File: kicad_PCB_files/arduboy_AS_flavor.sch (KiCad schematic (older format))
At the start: 70 parts, among them J1 USB_B_Micro, Q1 Si2301CDS, Q2 2N7002, SW1 RST Button, SW2 UP Button, SW3 DOWN Button, SW4 LEFT Button, SW5 RIGHT Button, SW6 RIGHT Button, SW7 RIGHT Button, SW8 ON Button, U1A1 ATmega32U4-AU, U1B1 ATmega32U4-MU, U2 TP4054, U3 W25Q128JVSIQ, Y1 16MHz

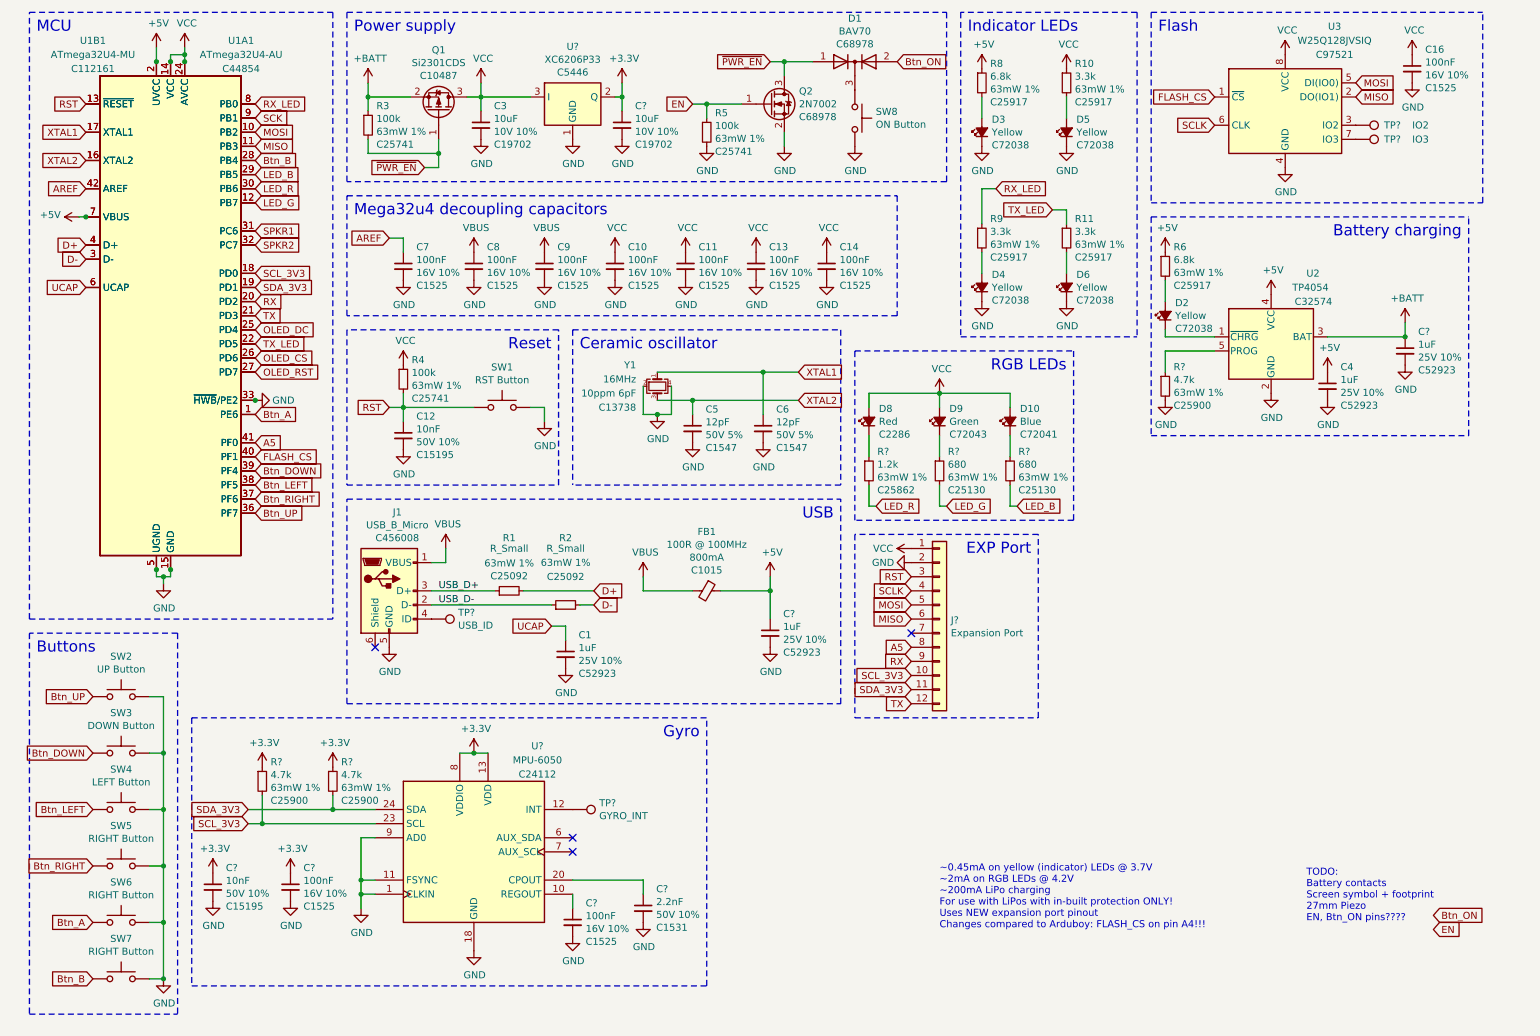
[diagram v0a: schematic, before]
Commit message: Multiple schematic changes Added SSH1106 connector (30 pin 0.7mm pitch)
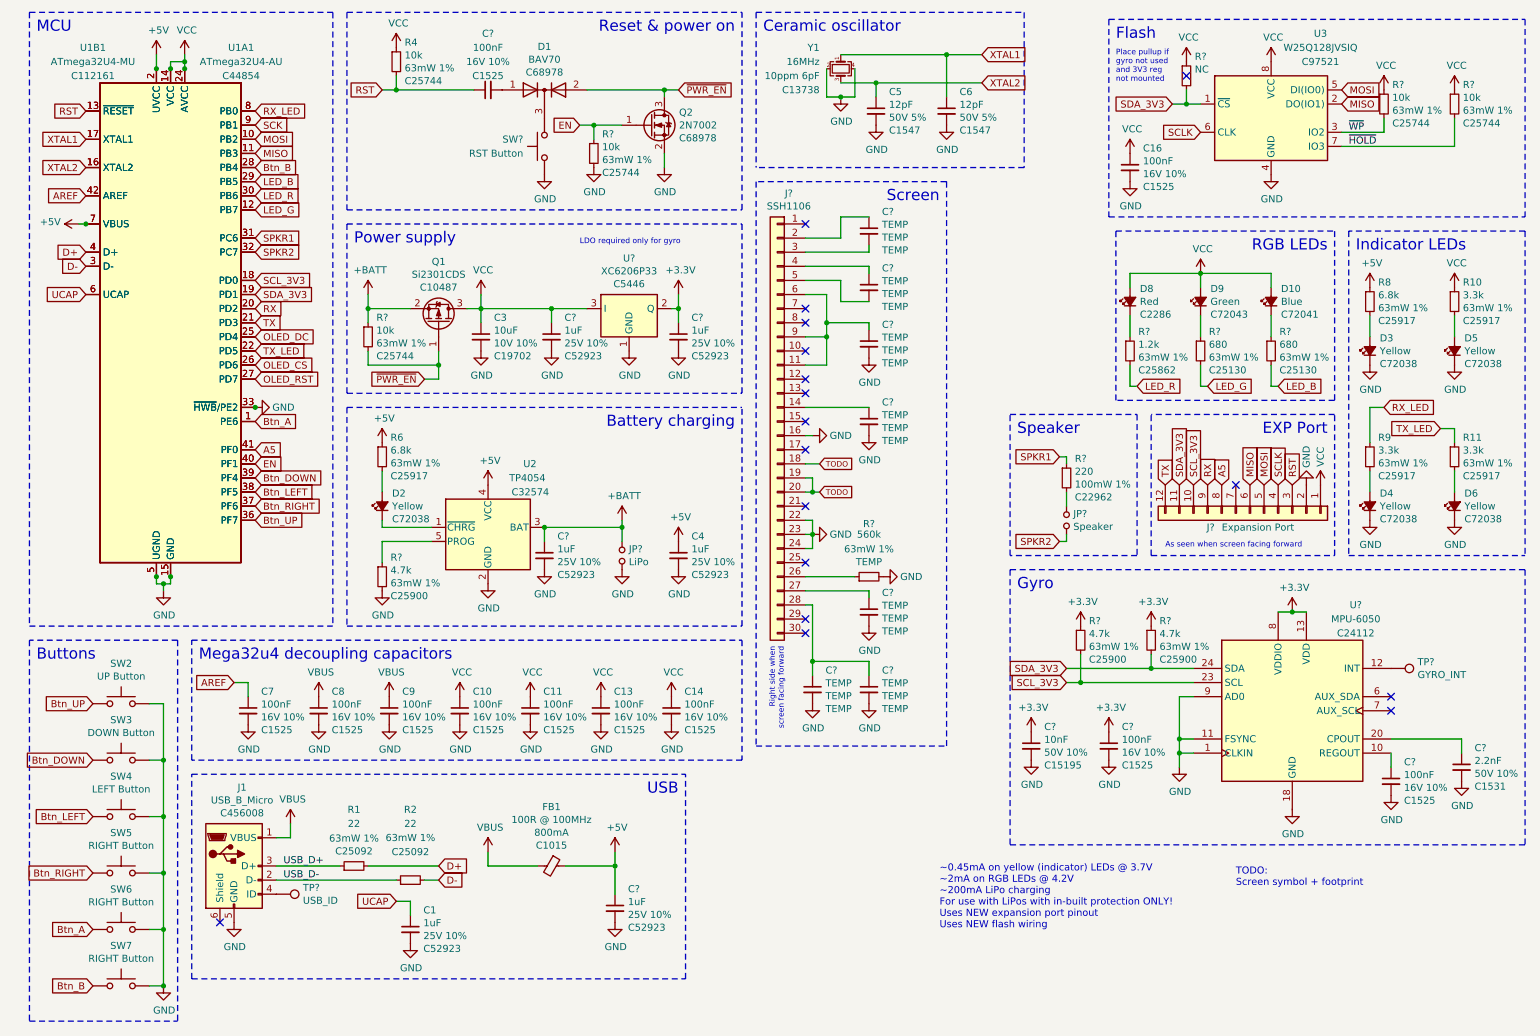
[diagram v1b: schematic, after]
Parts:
- removed C12: 10nF, Capacitor_SMD:C_0402_1005Metric_Pad0.74x0.62mm_HandSolder, symbol Device:C_Small
- removed C?: 10uF, Capacitor_SMD:C_0603_1608Metric_Pad1.08x0.95mm_HandSolder, symbol Device:C_Small
- removed R3, R5: 100k, Resistor_SMD:R_0402_1005Metric_Pad0.72x0.64mm_HandSolder, symbol Device:R_Small
- removed SW1: RST Button, arduboy:button_TS-1187A-B-A-B, symbol Switch:SW_Push
- removed SW8: ON Button, arduboy:button_TS-1187A-B-A-B, symbol Switch:SW_Push
- removed TP?: IO2, symbol Connector:TestPoint
- removed TP?: IO3, symbol Connector:TestPoint
- added C?: 100nF, Capacitor_SMD:C_0402_1005Metric_Pad0.74x0.62mm_HandSolder, symbol Device:C_Small
- added C? (x2): 1uF, Capacitor_SMD:C_0402_1005Metric_Pad0.74x0.62mm_HandSolder, symbol Device:C_Small
- added C? (x7): TEMP, Capacitor_SMD:C_0402_1005Metric_Pad0.74x0.62mm_HandSolder, symbol Device:C_Small
- added J?: SSH1106, arduboy:SSH1106_30pin_P0.7mm, symbol Connector_Generic:Conn_01x30
- added JP?: Speaker, symbol Device:Jumper_NO_Small
- added JP?: LiPo, symbol Device:Jumper_NO_Small
- added R?: NC, Resistor_SMD:R_0402_1005Metric_Pad0.72x0.64mm_HandSolder, symbol Device:R_Small
- added R? (x4): 10k, Resistor_SMD:R_0402_1005Metric_Pad0.72x0.64mm_HandSolder, symbol Device:R_Small
- added R?: 220, Resistor_SMD:R_0603_1608Metric_Pad0.98x0.95mm_HandSolder, symbol Device:R_Small
- added R?: 560k, Resistor_SMD:R_0402_1005Metric_Pad0.72x0.64mm_HandSolder, symbol Device:R_Small
- added SW?: RST Button, arduboy:button_TS-1187A-B-A-B, symbol Switch:SW_Push
- R1, R2: value R_Small -> 22
- R4: value 100k -> 10k; LCSC C25741 -> C25744
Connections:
- net Btn_ON is gone; now on net ~PWR_EN: D1.2 (A)
- net +3V3: now also C?.1
- net +BATT: now also JP?.2, R?.1
- net EN: now also U1A1.40 (PF1), U1B1.40 (PF1), R?.1
- net GND: now also C?.2, C?.2, C?.2, C?.2, C?.2, C?.2, C?.2, J?.16 (Pin_16), J?.22 (Pin_22), J?.23 (Pin_23), J?.24 (Pin_24), JP?.1, R?.2, R?.2, SW?.1
- net RST: now also C?.1
- net SDA_3V3: now also U3.1 (~CS), R?.2
- net SPKR1: now also R?.1
- net SPKR2: now also JP?.1
- net VCC: now also C?.1, R?.1, R?.1, R?.1
- net ~PWR_EN: now also R?.2; no longer D1.1 (A)
- net ~WP: now reaches U3.3 (IO2)
- net ~WP: now also R?.2
- net ~HOLD: now reaches U3.7 (IO3)
- net ~HOLD: now also R?.2
- net at D1.3 (K): now also SW?.2
- removed net FLASH_CS: U1A1.40 (PF1), U1B1.40 (PF1), U3.1 (~CS)
- new net: C?.2, D1.1 (A)
- new net: JP?.2, R?.2
- new net: C?.1, J?.11 (Pin_11), J?.6 (Pin_6), J?.9 (Pin_9)
- new net: C?.1, J?.14 (Pin_14)
- new net: C?.1, J?.2 (Pin_2)
- new net: J?.26 (Pin_26), R?.1
- new net: C?.1, J?.27 (Pin_27)
- new net: C?.1, C?.1, J?.28 (Pin_28)
- new net: C?.2, J?.3 (Pin_3)
- new net: C?.1, J?.4 (Pin_4)
- new net: C?.2, J?.5 (Pin_5)
- new net TODO: J?.18 (Pin_18), J?.19 (Pin_19), J?.20 (Pin_20)
- no-connect marks 4 -> 17
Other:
- note added: "As seen when screen facing forward"
- note added: "LDO required only for gyro"
- note added: "Place pullup if\ngyro not used\nand 3V3 reg\nnot mounted"
- note added: "Reset & power on"
- note added: "Right side when\nscreen facing forward"
- note added: "Screen"
- note added: "Speaker"
- note added: "TODO:\nScreen symbol + footprint"
- note added: "~~0.45mA on yellow (indicator) LEDs @ 3.7V\n~~2mA on RGB LEDs @ 4.2V\n~~200mA LiPo charging\nFor use with LiPos with in-built protection ONLY!\nUses NEW expansion port pinout\nUses NEW flash wiring"
- note removed: "Reset"
- note removed: "TODO:\nBattery contacts\nScreen symbol + footprint\n27mm Piezo\nEN, Btn_ON pins????"
- note removed: "~~0.45mA on yellow (indicator) LEDs @ 3.7V\n~~2mA on RGB LEDs @ 4.2V\n~~200mA LiPo charging\nFor use with LiPos with in-built protection ONLY!\nUses NEW expansion port pinout\nChanges compared to Arduboy: FLASH_CS on pin A4!!!"
- moved on the sheet: C1, C10, C11, C13, C14, C16, C3, C4, C5, C6, C7, C8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

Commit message: v0.1 schematic Added screen connectors Added testpoints Exported v0.1 schematic as .pdf
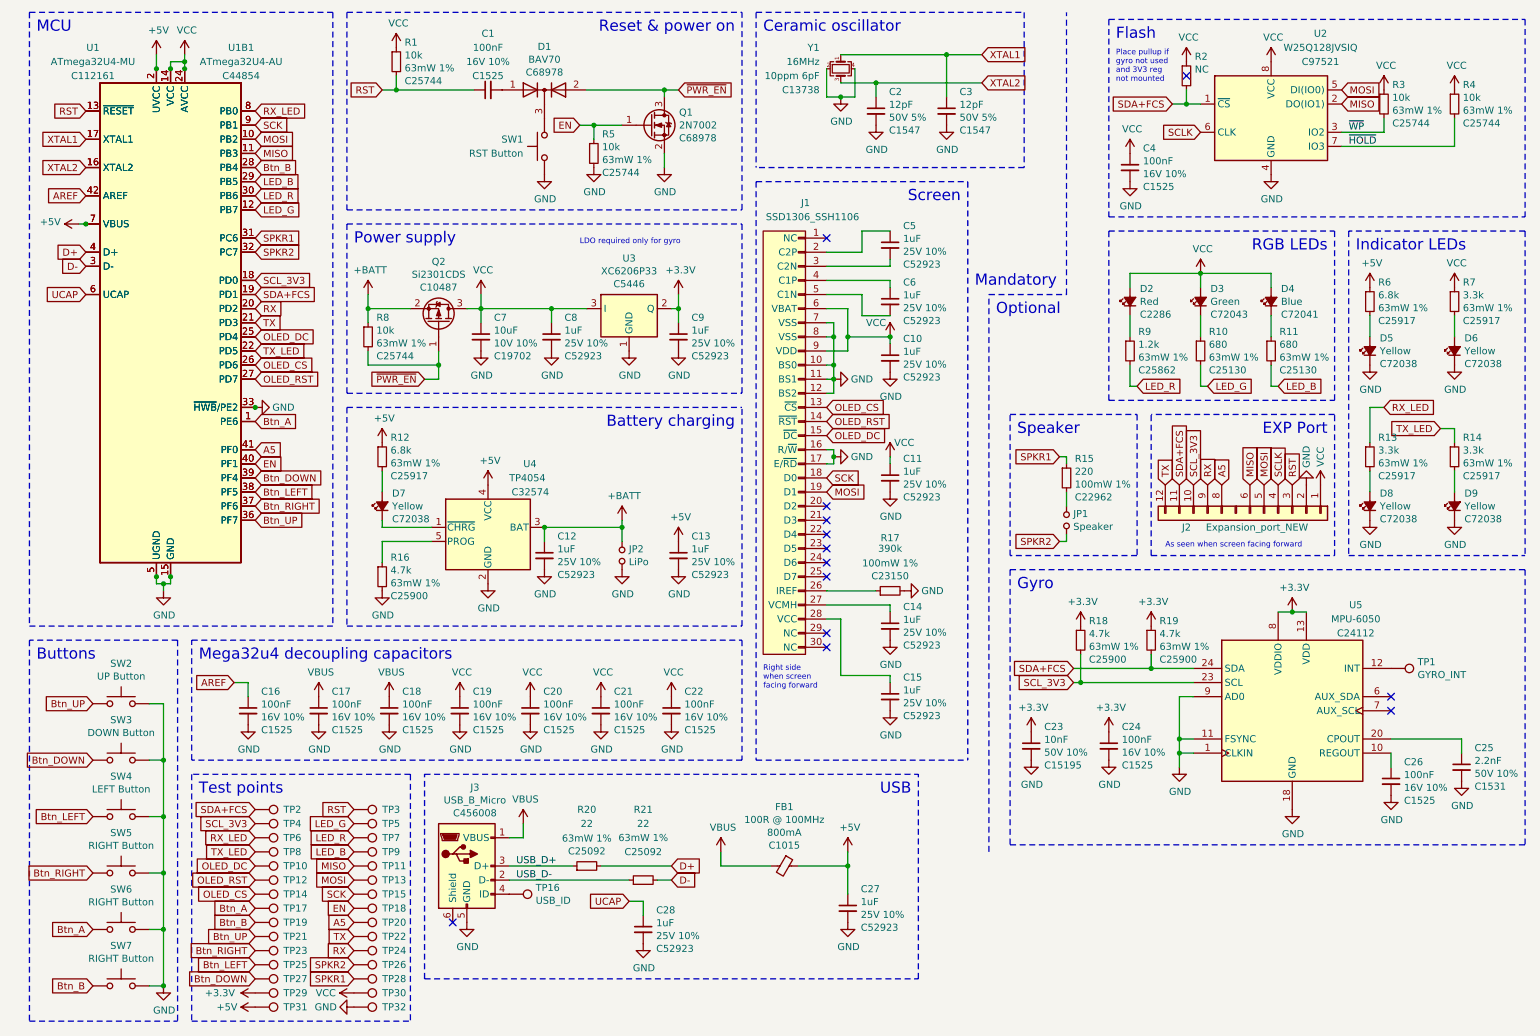
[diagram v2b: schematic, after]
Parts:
- removed C? (x7): TEMP, Capacitor_SMD:C_0402_1005Metric_Pad0.74x0.62mm_HandSolder, symbol Device:C_Small
- removed J?: SSH1106, arduboy:SSH1106_30pin_P0.7mm, symbol Connector_Generic:Conn_01x30
- removed J?: Expansion Port, symbol Connector_Generic:Conn_01x12
- added C10, C11, C14, C15, C5, C6: 1uF, Capacitor_SMD:C_0402_1005Metric_Pad0.74x0.62mm_HandSolder, symbol Device:C_Small
- added J1: SSD1306_SSH1106, arduboy:SSH1106_30pin_P0.7mm, symbol arduboy:SSD1306_SSH1106_30pin_soldered
- added J2: Expansion_port_NEW, arduboy:PinHeader_1x12_P2.54mm_SLOTTED_ROTATED, symbol arduboy:Expansion_port_NEW
- added TP10: D4/D4/~OLED_DC, symbol Connector:TestPoint
- added TP11: D14/PB3/MISO, symbol Connector:TestPoint
- added TP12: D6/D7/~OLED_RST, symbol Connector:TestPoint
- added TP13: D16/PB2/MOSI, symbol Connector:TestPoint
- added TP14: D12/D6/~OLED_CS, symbol Connector:TestPoint
- added TP15: D15/PB1/SCK, symbol Connector:TestPoint
- added TP17: D7/E6/A, symbol Connector:TestPoint
- added TP18: A4/F1/EN, symbol Connector:TestPoint
- added TP19: D8/PB4/B, symbol Connector:TestPoint
- added TP2: D2/PD1/SDA+FLASH_CS, symbol Connector:TestPoint
- added TP20: A5/F0, symbol Connector:TestPoint
- added TP21: A0/PF7/UP, symbol Connector:TestPoint
- added TP22: D1/PD3/TX, symbol Connector:TestPoint
- added TP23: A1/F6/RIGHT, symbol Connector:TestPoint
- added TP24: D0/PD2/RX, symbol Connector:TestPoint
- added TP25: A2/F5/LEFT, symbol Connector:TestPoint
- added TP26: D13/PC7/SPKR2, symbol Connector:TestPoint
- added TP27: A3/F4/DOWN, symbol Connector:TestPoint
- added TP28: D5/PC6/SPKR1, symbol Connector:TestPoint
- added TP29: 3V3, symbol Connector:TestPoint
- added TP3: ~RST, symbol Connector:TestPoint
- added TP30: VCC, symbol Connector:TestPoint
- added TP31: 5V_USB, symbol Connector:TestPoint
- added TP32: GND, symbol Connector:TestPoint
- added TP4: D3/PD0/SCL, symbol Connector:TestPoint
- added TP5: D11/PB7/~LED_G, symbol Connector:TestPoint
- added TP6: D17/PB0/~RX_LED, symbol Connector:TestPoint
- added TP7: D10/PB6/~LED_R, symbol Connector:TestPoint
- added TP8: D30/D5/~TX_LED, symbol Connector:TestPoint
- added TP9: D9/PB5/~LED_B, symbol Connector:TestPoint
- R17: renamed from R?; value 560k -> 390k; footprint Resistor_SMD:R_0402_1005Metric_Pad0.72x0.64mm_HandSolder -> Resistor_SMD:R_0603_1608Metric_Pad0.98x0.95mm_HandSolder; LCSC TEMP -> C23150; Rating 63mW 1% -> 100mW 1%
- gave numbers to parts that had none: 28
- renumbered C4 to C13, C7 to C16, C8 to C17, C9 to C18, C10 to C19, C5 to C2, C11 to C20, C13 to C21, C14 to C22, C1 to C28, C6 to C3, C16 to C4, C3 to C7, D8 to D2, D9 to D3, D10 to D4, D3 to D5, D5 to D6, D2 to D7, D4 to D8, D6 to D9, J1 to J3, Q2 to Q1, Q1 to Q2, R4 to R1, R6 to R12, R9 to R13, R11 to R14, R1 to R20, R2 to R21, R8 to R6, R10 to R7, U1B1 to U1, U1A1 to U1B1, U3 to U2, U2 to U4
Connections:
- net +3V3: now also TP29.1
- net +5V: now also TP31.1
- net A5: now also J2.8 (Pin_8), TP20.1
- net Btn_A: now also TP17.1
- net Btn_B: now also TP19.1
- net Btn_DOWN: now also TP27.1
- net Btn_LEFT: now also TP25.1
- net Btn_RIGHT: now also TP23.1
- net Btn_UP: now also TP21.1
- net EN: now also TP18.1
- net GND: now also C10.2, C11.2, C14.2, C15.2, J1.10 (BS0), J1.11 (BS1), J1.12 (BS2), J1.16 (R/~W), J1.17 (E/~RD), J1.7 (VSS), J1.8 (VSS), J2.2 (Pin_2), TP32.1
- net LED_B: now also TP9.1
- net LED_G: now also TP5.1
- net LED_R: now also TP7.1
- net MISO: now also J2.6 (Pin_6), TP11.1
- net MOSI: now also J1.19 (D1), J2.5 (Pin_5), TP13.1
- net OLED_CS: now also J1.13 (~CS), TP14.1
- net OLED_DC: now also J1.15 (~DC), TP10.1
- net OLED_RST: now also J1.14 (~RST), TP12.1
- net RST: now also J2.3 (Pin_3), TP3.1
- net RX: now also J2.9 (Pin_9), TP24.1
- net RX_LED: now also TP6.1
- net SCK: now also J1.18 (D0), TP15.1
- net SCLK: now also J2.4 (Pin_4)
- net SCL_3V3: now also J2.10 (Pin_10), TP4.1
- net SPKR1: now also TP28.1
- net SPKR2: now also TP26.1
- net TX: now also J2.12 (Pin_12), TP22.1
- net TX_LED: now also TP8.1
- net VCC: now also C10.1, C11.1, J1.6 (VBAT), J1.9 (VDD), J2.1 (Pin_1), TP30.1
- net at R17.1: now also J1.26 (IREF)
- net SDA_3V3 renamed SDA+FCS
- net SDA+FCS: now also J2.11 (Pin_11), TP2.1
- new net: C14.1, J1.27 (VCMH)
- new net: C15.1, J1.28 (VCC)
- new net: C6.1, J1.4 (C1P)
- new net: C6.2, J1.5 (C1N)
- new net: C5.1, J1.2 (C2P)
- new net: C5.2, J1.3 (C2N)
- no-connect marks 17 -> 13
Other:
- note added: "Mandatory"
- note added: "Optional"
- note added: "Right side\nwhen screen\nfacing forward"
- note added: "Test points"
- note removed: "Right side when\nscreen facing forward"
- note removed: "TODO:\nScreen symbol + footprint"
- note removed: "~~0.45mA on yellow (indicator) LEDs @ 3.7V\n~~2mA on RGB LEDs @ 4.2V\n~~200mA LiPo charging\nFor use with LiPos with in-built protection ONLY!\nUses NEW expansion port pinout\nUses NEW flash wiring"
- moved on the sheet: C27, C28, FB1, J3, R17, R20, R21, TP16

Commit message: Changed screen capacitor's size and value PCB mockup added
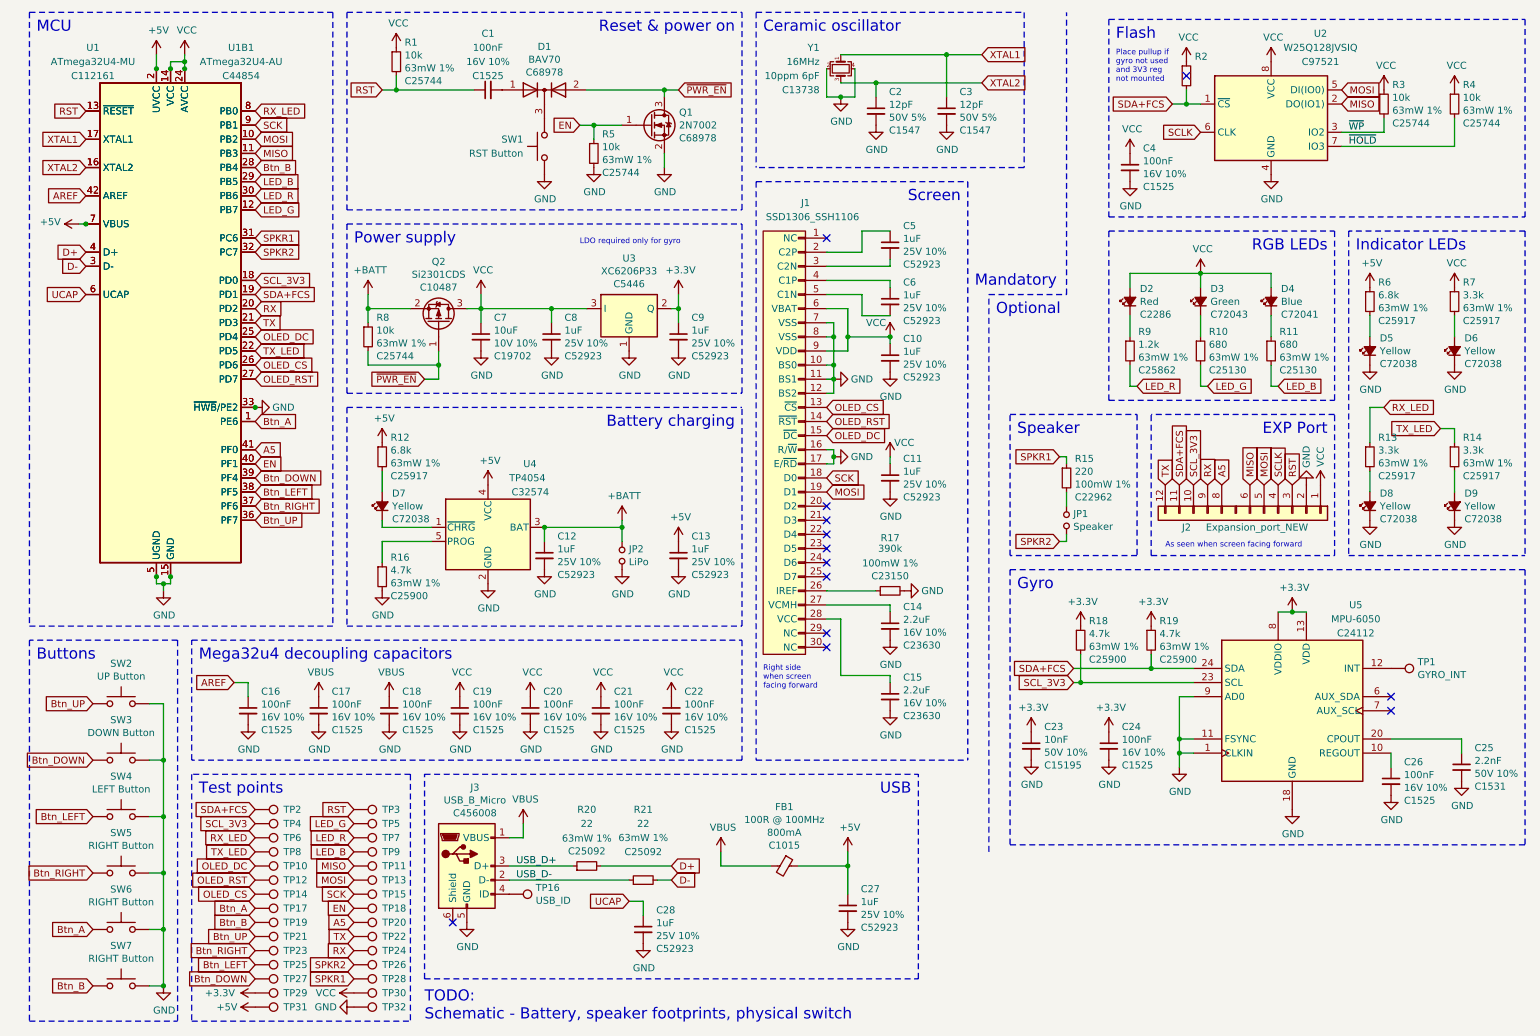
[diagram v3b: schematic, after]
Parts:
- C14, C15: value 1uF -> 2.2uF; footprint Capacitor_SMD:C_0402_1005Metric_Pad0.74x0.62mm_HandSolder -> Capacitor_SMD:C_0603_1608Metric_Pad1.08x0.95mm_HandSolder; LCSC C52923 -> C23630; Rating 25V 10% -> 16V 10%
- JP1, JP2: footprint (none) -> Connector_PinHeader_2.54mm:PinHeader_1x02_P2.54mm_Vertical
- R2: value NC -> 10k; LCSC (none) -> C25744-NC; Rating (none) -> 63mW 1%
- TP1, TP10, TP11, TP12, TP13, TP14, TP15, TP16, TP17, TP18, TP19, TP2, TP20, TP21, TP22, TP23, TP24, TP25, TP26, TP27, TP28, TP29, TP3, TP30, TP31, TP32, TP4, TP5, TP6, TP7, TP8, TP9: footprint (none) -> TestPoint:TestPoint_Pad_D2.0mm
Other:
- note added: "TODO:\nSchematic - Battery, speaker footprints, physical switch"
